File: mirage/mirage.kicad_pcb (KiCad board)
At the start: 2 copper layers, 39 x 26 mm, 7 parts, among them U1 STM32U575VGT6

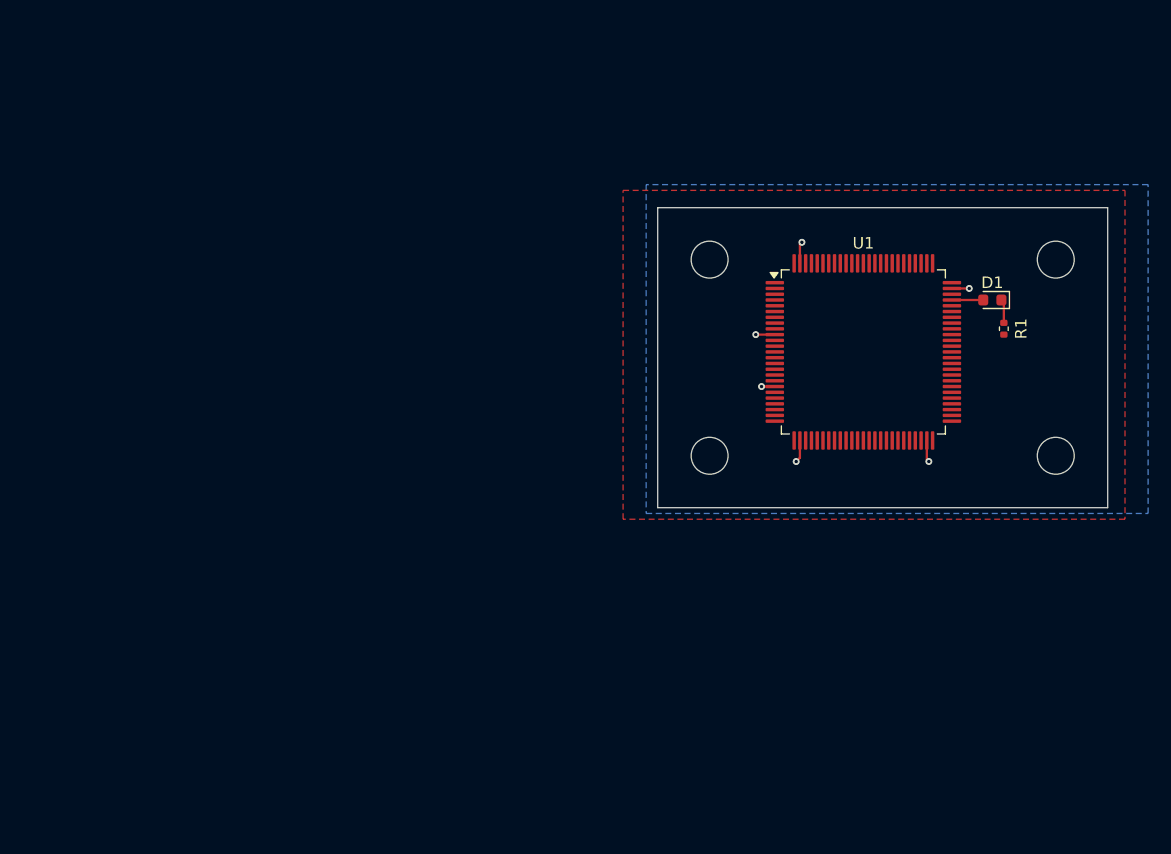
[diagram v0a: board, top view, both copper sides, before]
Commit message: feat(sensor): fundamental sensor lists
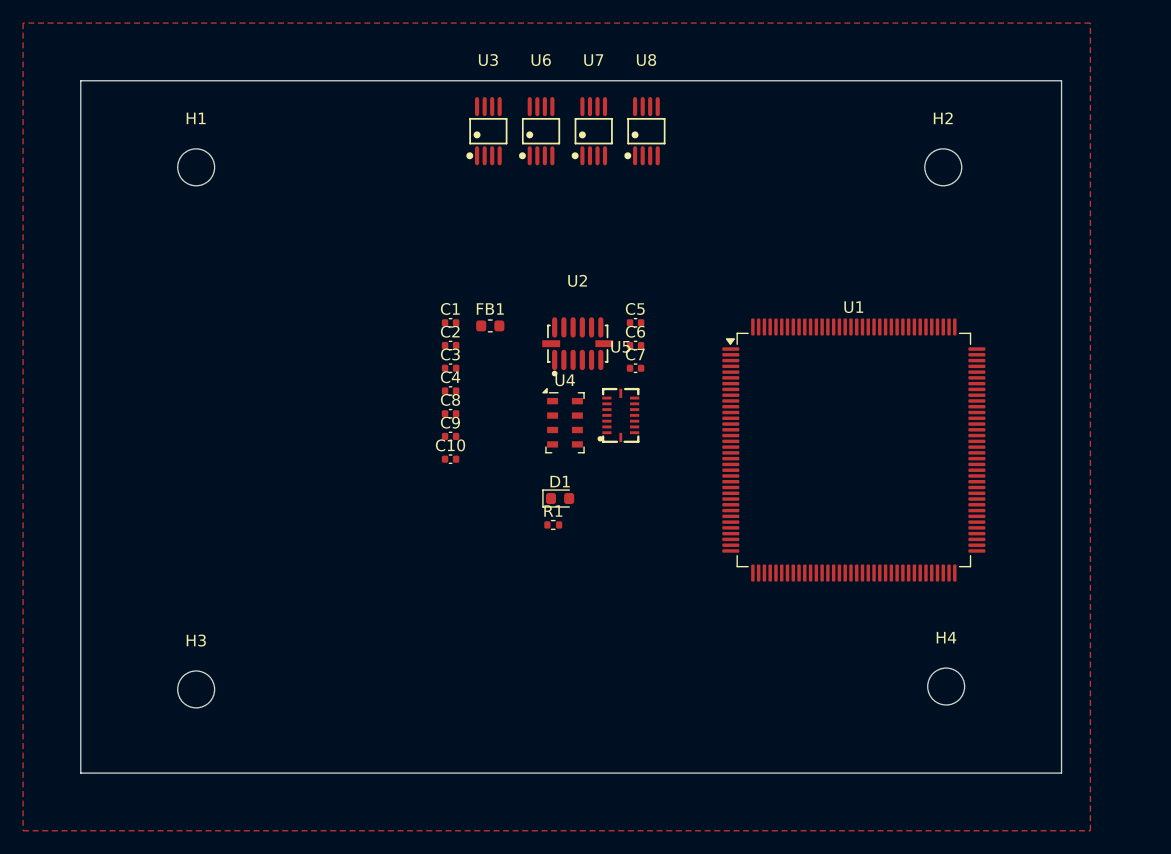
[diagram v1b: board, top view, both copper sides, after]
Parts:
- added C1: 100nF, Capacitor_SMD:C_0402_1005Metric, F.Cu at (92.0, 83.5)
- added C10: 10n, Capacitor_SMD:C_0402_1005Metric, F.Cu at (92.0, 95.3)
- added C2: 100nF, Capacitor_SMD:C_0402_1005Metric, F.Cu at (92.0, 85.4)
- added C3: 100nF, Capacitor_SMD:C_0402_1005Metric, F.Cu at (92.0, 87.4)
- added C4: 100nF, Capacitor_SMD:C_0402_1005Metric, F.Cu at (92.0, 89.4)
- added C5: 100nF, Capacitor_SMD:C_0402_1005Metric, F.Cu at (108.1, 83.5)
- added C6: 100nF, Capacitor_SMD:C_0402_1005Metric, F.Cu at (108.1, 85.4)
- added C7: 100nF, Capacitor_SMD:C_0402_1005Metric, F.Cu at (108.1, 87.4)
- added C8: 100n, Capacitor_SMD:C_0402_1005Metric, F.Cu at (92.0, 91.4)
- added C9: 10n, Capacitor_SMD:C_0402_1005Metric, F.Cu at (92.0, 93.3)
- added FB1: 120R, Inductor_SMD:L_0603_1608Metric, F.Cu at (95.5, 83.7)
- added U2: ADXL375BCCZ-RL7, EasyEDA:LGA-14_L5.0-W3.0-P0.80-BL, F.Cu at (103.1, 85.3)
- added U3: TMP275AIDGKR VSSOP8, EasyEDA:VSSOP-8_L3.0-W3.0-P0.65-LS5.0-BL, F.Cu at (95.3, 66.9)
- added U4: MS5607-02BA, Package_LGA:LGA-8_3x5mm_P1.25mm, F.Cu at (102.0, 92.1)
- added U5: BMI088, EasyEDA:LGA-16_L4.5-W3.0-P0.50-BL, F.Cu at (106.8, 91.5)
- added U6: TMP275AIDGKR VSSOP8, EasyEDA:VSSOP-8_L3.0-W3.0-P0.65-LS5.0-BL, F.Cu at (99.9, 66.9)
- added U7: TMP275AIDGKR VSSOP8, EasyEDA:VSSOP-8_L3.0-W3.0-P0.65-LS5.0-BL, F.Cu at (104.5, 66.9)
- added U8: TMP275AIDGKR VSSOP8, EasyEDA:VSSOP-8_L3.0-W3.0-P0.65-LS5.0-BL, F.Cu at (109.0, 66.9)
- U1: value STM32U575VGT6 -> STM32H573ZITx; footprint Package_QFP:LQFP-100_14x14mm_P0.5mm -> Package_QFP:LQFP-144_20x20mm_P0.5mm
- moved H3 77.2 mm to (70.0, 115.2)
- moved H1 45.2 mm to (70.0, 70.0)
- moved R1 42.6 mm to (101.0, 101.0), turned to 0 degrees
- moved D1 41.2 mm to (101.5, 98.7), turned to 0 degrees
- moved H4 28.6 mm to (135.0, 115.0)
- moved H2 12.6 mm to (134.8, 70.0)
- moved U1 8.54 mm to (127.0, 94.5)
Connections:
- U1 pad 10: GND -> unconnected-(U1-PF0-Pad10)
- U1 pad 100: +3.3V -> unconnected-(U1-PA8-Pad100)
- U1 pad 11: +3.3V -> unconnected-(U1-PF1-Pad11)
- U1 pad 16: unconnected-(U1-PC1-Pad16) -> GND
- U1 pad 17: unconnected-(U1-PC2-Pad17) -> +3.3V
- U1 pad 19: GND -> unconnected-(U1-PF7-Pad19)
- U1 pad 27: GND -> unconnected-(U1-PC1-Pad27)
- U1 pad 28: +3.3V -> unconnected-(U1-PC2-Pad28)
- U1 pad 30: unconnected-(U1-PA5-Pad30) -> +3.3V
- U1 pad 31: unconnected-(U1-PA6-Pad31) -> GND
- U1 pad 33: unconnected-(U1-PC4-Pad33) -> +3.3VA
- U1 pad 38: unconnected-(U1-PE7-Pad38) -> GND
- U1 pad 39: unconnected-(U1-PE8-Pad39) -> +3.3V
- U1 pad 49: GND -> unconnected-(U1-PF11-Pad49)
- U1 pad 50: +3.3V -> unconnected-(U1-PF12-Pad50)
- U1 pad 51: unconnected-(U1-PB12-Pad51) -> GND
- U1 pad 52: unconnected-(U1-PB13-Pad52) -> +3.3V
- U1 pad 61: unconnected-(U1-PD14-Pad61) -> GND
- U1 pad 62: unconnected-(U1-PD15-Pad62) -> +3.3V
- U1 pad 71: unconnected-(U1-PA12-Pad71) -> GND
- U1 pad 72: YELLOW_LED -> +3.3V
- U1 pad 74: GND -> unconnected-(U1-PB13-Pad74)
- U1 pad 75: +3.3V -> unconnected-(U1-PB14-Pad75)
- U1 pad 83: unconnected-(U1-PD2-Pad83) -> GND
- U1 pad 84: unconnected-(U1-PD3-Pad84) -> +3.3V
- U1 pad 94: unconnected-(U1-PH3-Pad94) -> GND
- U1 pad 95: unconnected-(U1-PB8-Pad95) -> +3.3V
- U1 pad 99: GND -> unconnected-(U1-PC9-Pad99)
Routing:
- net GND: track 10.1 -> 0.00 mm, vias 6 -> 0
- net YELLOW_LED: track 2.71 -> 0.00 mm
- net Net-(D1-K): track 2.07 -> 0.00 mm
- removed copper zone on B.Cu, net GND
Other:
- board size 39 x 26 mm -> 85 x 60 mm

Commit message: feat: connectors
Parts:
- added C11: 100nF, Capacitor_SMD:C_0402_1005Metric, F.Cu at (83.0, 82.2)
- added C12: 100nF, Capacitor_SMD:C_0402_1005Metric, F.Cu at (85.0, 83.5)
- added C13: 10uF, Capacitor_SMD:C_0402_1005Metric, F.Cu at (83.0, 86.1)
- added C14: 100nF, Capacitor_SMD:C_0402_1005Metric, F.Cu at (83.0, 88.1)
- added C15: 100nF, Capacitor_SMD:C_0402_1005Metric, F.Cu at (83.0, 90.0)
- added C16: 100nF, Capacitor_SMD:C_0504_1310Metric_Pad0.83x1.28mm_HandSolder, F.Cu at (87.4, 78.5)
- added C17: 100nF, Capacitor_SMD:C_0402_1005Metric, F.Cu at (83.0, 92.0)
- added R2: 5k, Resistor_SMD:R_0402_1005Metric, F.Cu at (85.9, 82.2)
- added R3: 5k, Resistor_SMD:R_0402_1005Metric, F.Cu at (85.9, 84.2)
- moved C5 9.69 mm to (117.7, 82.3)
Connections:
- U3 pad 3: /Sensors/TMP275_ALERT -> TMP275_ALERT0
- U6 pad 3: /Sensors/TMP275_ALERT -> TMP275_ALERT2
- U7 pad 3: /Sensors/TMP275_ALERT -> TMP275_ALERT1
- U8 pad 3: /Sensors/TMP275_ALERT -> TMP275_ALERT3
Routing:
- net Net-(U2-VDDI/O): track 0.00 -> 18.1 mm, vias 0 -> 2
- net GND: track 0.00 -> 5.91 mm
